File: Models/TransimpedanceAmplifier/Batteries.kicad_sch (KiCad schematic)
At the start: 2 parts

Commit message: Save progress
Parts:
- BT1, BT2: Cost $0.00 -> (none); RoHS Compliant NO -> (none)
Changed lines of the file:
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@@
 			)
 		)
-		(property "Cost" "$0.00"
+		(property "Cost" ""
 			(at 170.18 62.23 0)
 			(effects
@@
 			)
 		)
-		(property "RoHS Compliant" "NO"
+		(property "RoHS Compliant" ""
 			(at 170.18 62.23 0)
 			(effects
@@
 			)
 		)
-		(property "Cost" "$0.00"
+		(property "Cost" ""
 			(at 170.18 110.49 0)
 			(effects
@@
 			)
 		)
-		(property "RoHS Compliant" "NO"
+		(property "RoHS Compliant" ""
 			(at 170.18 110.49 0)
 			(effects

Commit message: Added important links regarding high-voltage electronics
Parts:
- BT1, BT2: now left out of the parts list
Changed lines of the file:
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@@
 		(unit 1)
 		(exclude_from_sim no)
-		(in_bom yes)
+		(in_bom no)
 		(on_board yes)
 		(dnp no)
@@
 		)
 		(property "RoHS Compliant" ""
+			(at 170.18 62.23 0)
+			(effects
+				(font
+					(size 1.27 1.27)
+				)
+				(hide yes)
+			)
+		)
+		(property "Purchase Link" ""
 			(at 170.18 62.23 0)
 			(effects
@@
 		(unit 1)
 		(exclude_from_sim no)
-		(in_bom yes)
+		(in_bom no)
 		(on_board yes)
 		(dnp no)
@@
 			(at 170.18 110.49 0)
 			(effects
+				(font
+					(size 1.27 1.27)
+				)
+				(hide yes)
+			)
+		)
+		(property "Purchase Link" ""
+			(at 170.18 110.49 0)
+			(effects

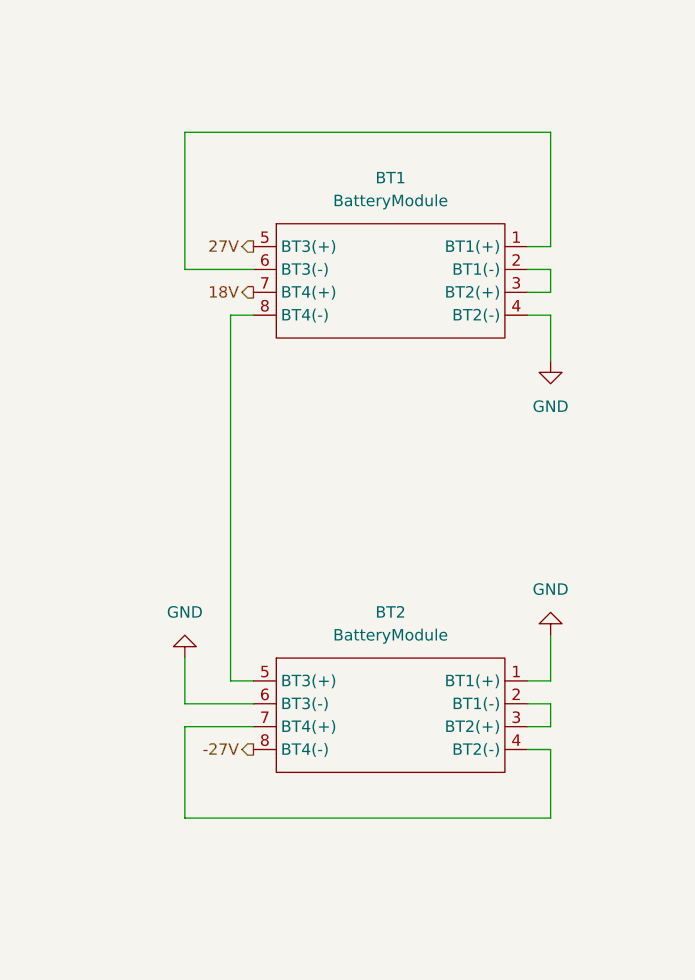
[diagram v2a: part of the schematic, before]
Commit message: Rewired the battery modules
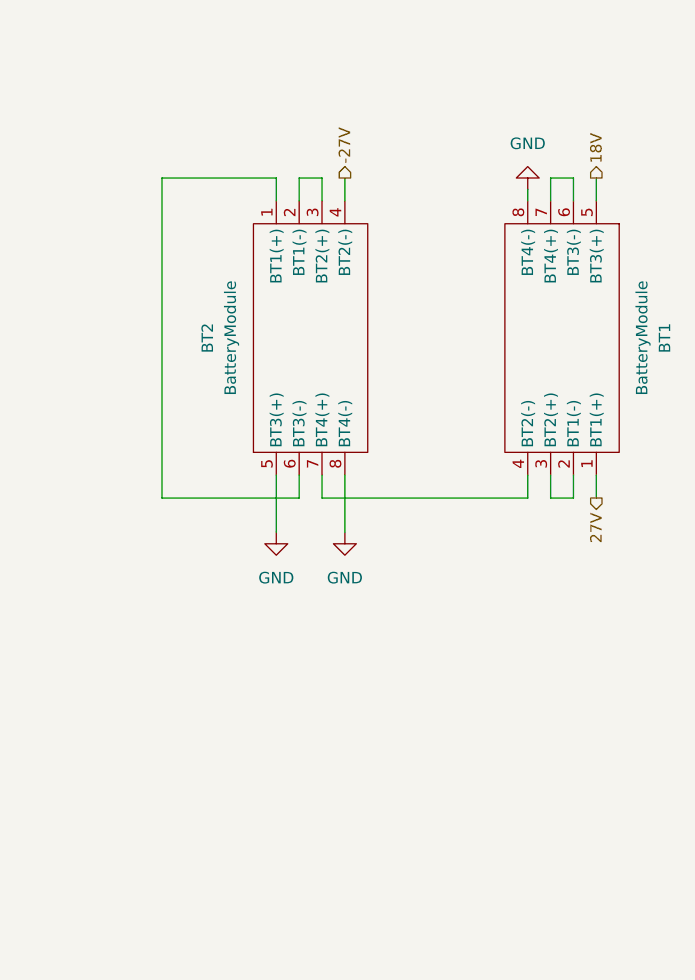
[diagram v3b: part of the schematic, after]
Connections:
- net -27V: now also BT2.4 (BT2(-)); no longer BT2.8 (BT4(-))
- net 18V: now also BT1.5 (BT3(+)); no longer BT1.7 (BT4(+))
- net 27V: now also BT1.1 (BT1(+)); no longer BT1.5 (BT3(+))
- net GND: now also BT1.8 (BT4(-)), BT2.5 (BT3(+)), BT2.8 (BT4(-)); no longer BT1.4 (BT2(-)), BT2.1 (BT1(+)), BT2.6 (BT3(-))
- net at BT1.6 (BT3(-)): now also BT1.7 (BT4(+)); no longer BT1.1 (BT1(+))
- net at BT2.7 (BT4(+)): now also BT1.4 (BT2(-)); no longer BT2.4 (BT2(-))
- new net: BT2.1 (BT1(+)), BT2.6 (BT3(-))
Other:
- moved on the sheet: BT1, BT2
